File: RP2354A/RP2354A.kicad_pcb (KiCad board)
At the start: 2 copper layers, 40 x 80 mm, 66 parts, among them J101 USB4085-GF-A, J102 AudioJack2_SwitchT, J103 AudioJack2_SwitchT, J201 TC2030-NL, Q101 MMBF5103, SW201 SW_Push_DPDT, U201 RP2354A, U202 NCP1117-3.3_SOT223, U301 TAC5112, Y201 ABM8-272-T3

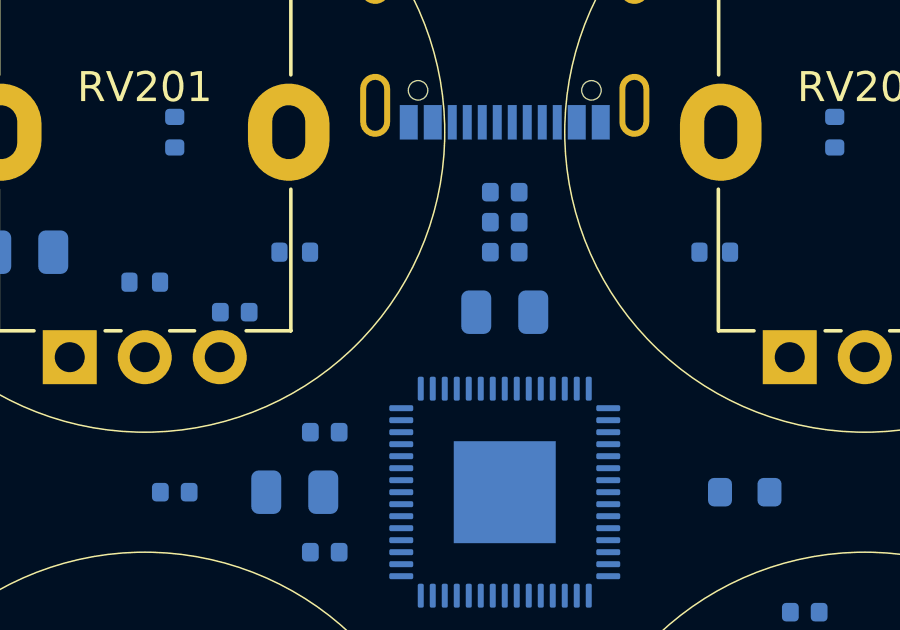
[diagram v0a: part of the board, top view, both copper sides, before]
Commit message: Update RP2354 board with proper inductor symbol
.. and fix up the LED simulation a bit too.  I simulate LEDs with the
built-in diode model, but with N ("emission coefficient") set to 3,
which gets me a forward voltage around 2V.

But I think I should change RS ("series resistance") instead (or in
addition to).  See

    https://led-ld.nichia.co.jp/api/data/spec/tech/SP-QR-C2-210932-2-E_The%20SPICE%20Model%20of%20LEDs.pdf

which talks much more about this.

I guess I don't care that much, I just wanted the current simulation for
the power LED to be in roughly the right ballpark.

The inductor change is the relatively important thing here.

Signed-off-by: Linus Torvalds <torvalds@linux-foundation.org>
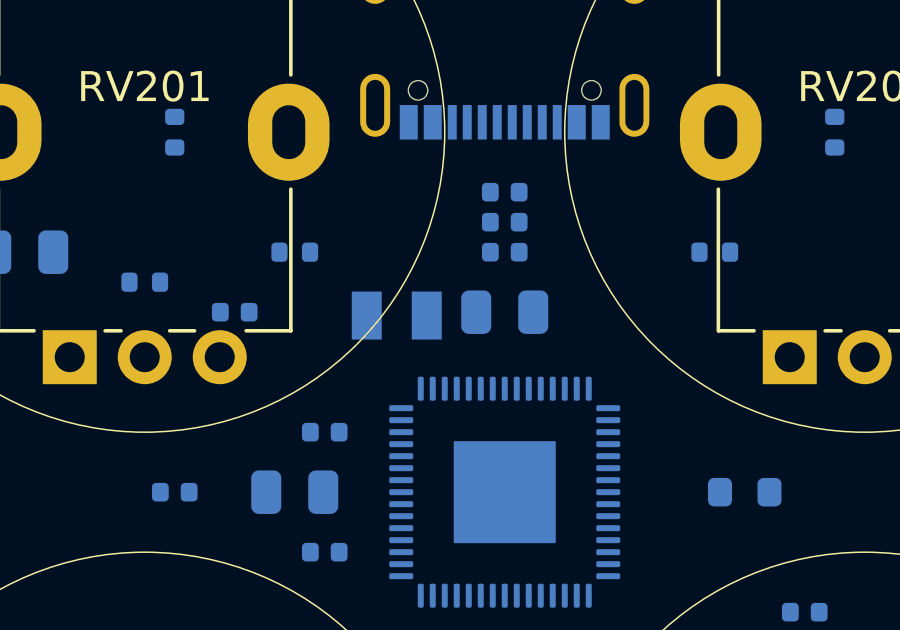
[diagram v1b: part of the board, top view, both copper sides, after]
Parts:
- added L201: 3.3u, Mylib:AOTA-B2016, B.Cu at (96.4, 84.1)
- turned C302 to 0 degrees
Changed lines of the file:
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@@
 			)
 		)
+		(property "Sim.Device" "D"
+			(at 0 0 0)
+			(unlocked yes)
+			(layer "F.Fab")
+			(hide yes)
+			(effects
+				(font
+					(size 1 1)
+					(thickness 0.15)
+				)
+			)
+		)
+		(property "Sim.Params" "n=3"
+			(at 0 0 0)
+			(unlocked yes)
+			(layer "F.Fab")
+			(hide yes)
+			(effects
+				(font
+					(size 1 1)
+					(thickness 0.15)
+				)
+			)
+		)
 		(property ki_fp_filters "LED* LED_SMD:* LED_THT:*")
 		(sheetname "/RPi/")
@@
 			)
 		)
-		(property "Sim.Params" "n=2.6"
+		(property "Sim.Params" "n=3"
 			(at 0 0 0)
 			(unlocked yes)
@@
 		(placed yes)
 		(layer "B.Cu")
-		(at 100 84 180)
+		(at 100 84)
 		(descr "Capacitor SMD 0805 (2012 Metric), square (rectangular) end terminal, IPC-7351 nominal, (Body size source: IPC-SM-782 page 76, https://www.pcb-3d.com/wordpress/wp-content/uploads/ipc-sm-782a_amendment_1_and_2.pdf, https://docs.google.com/spreadsheets/d/1BsfQQcO9C6DZCsRaXUlFlo91Tg2WpOkGARC1WS5S8t0/edit?usp=sharing), generated with kicad-footprint-generator")
 		(tags "capacitor")
@@
 		(attr smd)
 		(fp_line
-			(start -0.261252 0.735)
-			(end 0.261252 0.735)
+			(start -0.261252 -0.735)
+			(end 0.261252 -0.735)
 			(stroke
 				(width 0.12)
@@
 		)
 		(fp_line
-			(start -0.261252 -0.735)
-			(end 0.261252 -0.735)
+			(start -0.261252 0.735)
+			(end 0.261252 0.735)
 			(stroke
 				(width 0.12)
@@
 		)
 		(fp_line
-			(start 1.7 0.98)
-			(end 1.7 -0.98)
+			(start -1.7 -0.98)
+			(end -1.7 0.98)
 			(stroke
 				(width 0.05)
@@
 		)
 		(fp_line
-			(start 1.7 -0.98)
-			(end -1.7 -0.98)
+			(start -1.7 0.98)
+			(end 1.7 0.98)
 			(stroke
 				(width 0.05)
@@
 		)
 		(fp_line
-			(start -1.7 0.98)
-			(end 1.7 0.98)
+			(start 1.7 -0.98)
+			(end -1.7 -0.98)
 			(stroke
 				(width 0.05)
@@
 		)
 		(fp_line
-			(start -1.7 -0.98)
-			(end -1.7 0.98)
+			(start 1.7 0.98)
+			(end 1.7 -0.98)
 			(stroke
 				(width 0.05)
@@
 		)
 		(fp_line
-			(start 1 0.625)
-			(end 1 -0.625)
+			(start -1 -0.625)
+			(end -1 0.625)
 			(stroke
 				(width 0.1)
@@
 		)
 		(fp_line
-			(start 1 -0.625)
-			(end -1 -0.625)
+			(start -1 0.625)
+			(end 1 0.625)
 			(stroke
 				(width 0.1)
@@
 		)
 		(fp_line
-			(start -1 0.625)
-			(end 1 0.625)
+			(start 1 -0.625)
+			(end -1 -0.625)
 			(stroke
 				(width 0.1)
@@
 		)
 		(fp_line
-			(start -1 -0.625)
-			(end -1 0.625)
+			(start 1 0.625)
+			(end 1 -0.625)
 			(stroke
 				(width 0.1)
@@
 		)
 		(pad "1" smd roundrect
-			(at -0.95 0 180)
+			(at -0.95 0)
 			(size 1 1.45)
 			(layers "B.Cu" "B.Mask" "B.Paste")
@@
 		)
 		(pad "2" smd roundrect
-			(at 0.95 0 180)
+			(at 0.95 0)
 			(size 1 1.45)
 			(layers "B.Cu" "B.Mask" "B.Paste")
@@
 		)
 	)
+	(footprint "Mylib:AOTA-B2016"
+		(layer "B.Cu")
+		(at 96.4 84.1125 180)
+		(descr "Abracon Polarized Inductor 0806 (2016 metric)")
+		(tags "Inductor 0806 2016")
+		(property "Reference" "L201"
+			(at 0 2 0)
+			(unlocked yes)
+			(layer "B.SilkS")
+			(effects
+				(font
+					(size 1 1)
+					(thickness 0.1)
+				)
+				(justify mirror)
+			)
+		)
+		(property "Value" "3.3u"
+			(at 0 -1 0)
+			(unlocked yes)
+			(layer "B.Fab")
+			(effects
+				(font
+					(size 1 1)
+					(thickness 0.15)
+				)
+				(justify mirror)
+			)
+		)
+		(property "Datasheet" "https://abracon.com/datasheets/AOTA-B201610S3R3-101-T.pdf"
+			(at 0 0 0)
+			(unlocked yes)
+			(layer "B.Fab")
+			(hide yes)
+			(effects
+				(font
+					(size 1 1)
+					(thickness 0.15)
+				)
+				(justify mirror)
+			)
+		)
+		(property "Description" "Inductor"
+			(at 0 0 0)
+			(unlocked yes)
+			(layer "B.Fab")
+			(hide yes)
+			(effects
+				(font
+					(size 1 1)
+					(thickness 0.15)
+				)
+				(justify mirror)
+			)
+		)
+		(property ki_fp_filters "Choke_* *Coil* Inductor_* L_*")
+		(sheetname "/RPi/")
+		(sheetfile "rpi2354.kicad_sch")
+		(attr smd)
+		(fp_circle
+			(center -0.9 1.3)
+			(end -0.75 1.3)
+			(stroke
+				(width 0.1)
+				(type solid)
+			)
+			(fill yes)
+			(layer "B.SilkS")
+		)
+		(fp_rect
+			(start -1.65 1.05)
+			(end 1.65 -1.05)
+			(stroke
+				(width 0.05)
+				(type solid)
+			)
+			(fill no)
+			(layer "B.CrtYd")
+		)
+		(fp_text user "${REFERENCE}"
+			(at 0 -2.5 0)
+			(unlocked yes)
+			(layer "B.Fab")
+			(effects
+				(font
+					(size 1 1)
+					(thickness 0.15)
+				)
+				(justify mirror)
+			)
+		)
+		(pad "1" smd rect
+			(at -1 0 180)
+			(size 1 1.6)
+			(layers "B.Cu" "B.Mask" "B.Paste")
+			(net 10 "+1V1")
+			(pinfunction "1")
+			(pintype "passive")
+		)
+		(pad "2" smd rect
+			(at 1 0 180)
+			(size 1 1.6)
+			(layers "B.Cu" "B.Mask" "B.Paste")
+			(net 53 "/RPi/VREG_LX")
+			(pinfunction "2")
+			(pintype "passive")
+		)
+		(embedded_fonts no)
+	)
 	(footprint "Capacitor_SMD:C_0805_2012Metric"

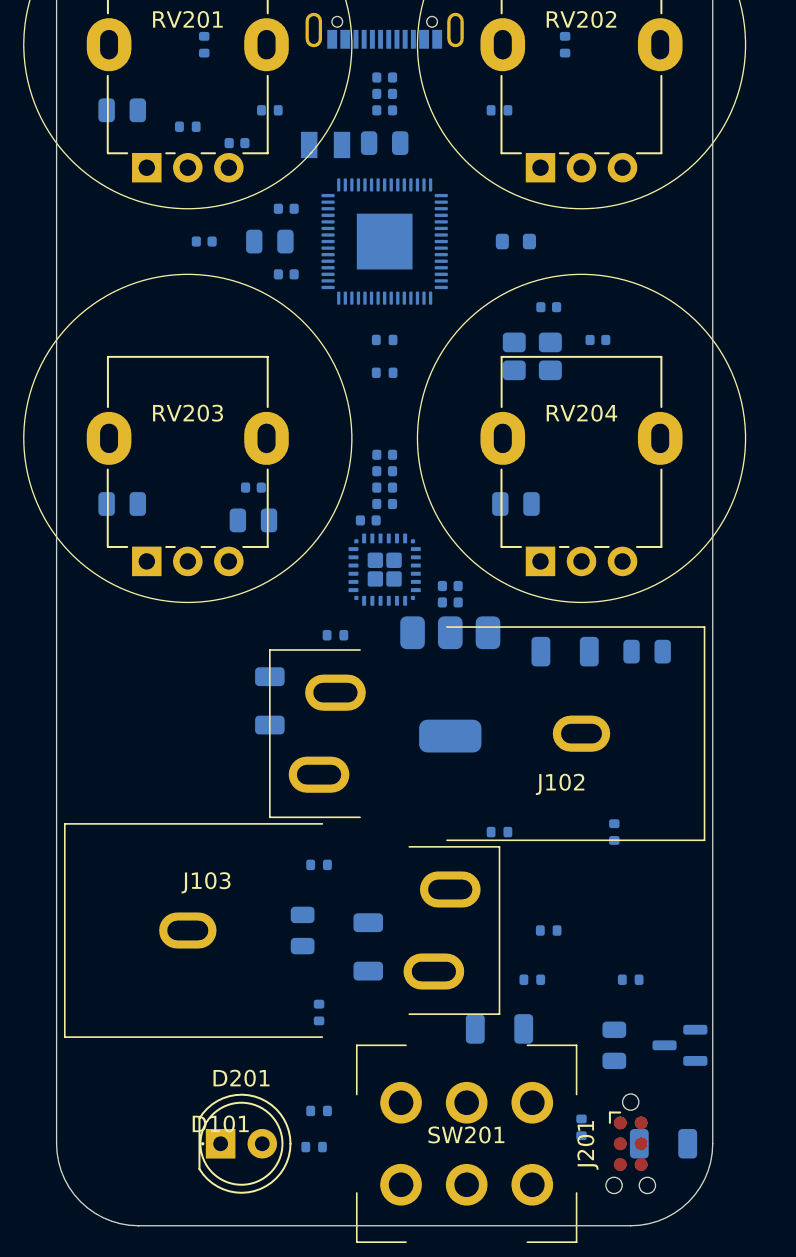
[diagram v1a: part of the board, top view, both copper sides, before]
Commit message: First cut at BOM selection for caps and resistors
The size choices were a bit random, this standardizes on 0402 for
resistors.  Also, optimize the BOM by just sharing values where they
don't matter that much.

For example, we need those 5k1 resistors for the USB CC pulldowns, and
we might as well then use that for the i2c pullup resistors too.  And
the self-biasing source resistor for the JFET input could use the same.

For similar reasons, just standardize on 33R for the low value resistors
that we use for the USB data line serial termination and the analog
voltage RC filtering.

Capacitors are 0402 for small values (0.1uF and smaller) or 0603 for
bigger capacitance values.  That seems to match availability.

Signed-off-by: Linus Torvalds <torvalds@linux-foundation.org>
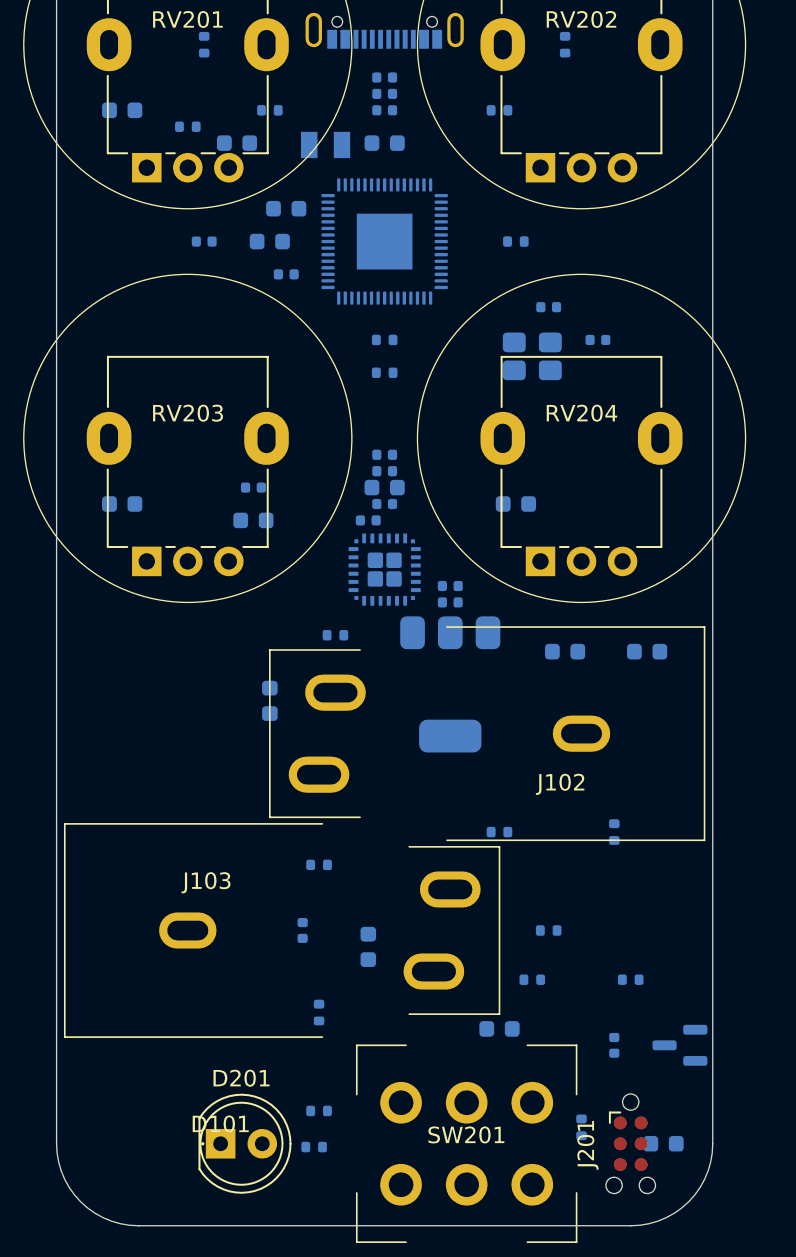
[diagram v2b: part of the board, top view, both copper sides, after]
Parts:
- C101, C103, C105, C106, C107: footprint Capacitor_SMD:C_1206_3216Metric -> Capacitor_SMD:C_0603_1608Metric
- C102, C104: footprint Capacitor_SMD:C_0805_2012Metric -> Capacitor_SMD:C_0402_1005Metric
- C201, C202: value 4.7u -> 4.7uF; footprint Capacitor_SMD:C_0805_2012Metric -> Capacitor_SMD:C_0603_1608Metric
- C203, C206, C207, C208, C209, C210, C211, C212, C213: value 100n -> 0.1uF
- C204, C205: value 4.7u -> 4.7uF; footprint Capacitor_SMD:C_0402_1005Metric -> Capacitor_SMD:C_0603_1608Metric
- C214, C215: value 15p -> 15pF
- C216, C217: value 10u -> 10uF; footprint Capacitor_SMD:C_0805_2012Metric -> Capacitor_SMD:C_0603_1608Metric
- C301, C302, C305: footprint Capacitor_SMD:C_0805_2012Metric -> Capacitor_SMD:C_0603_1608Metric
- C307: footprint Capacitor_SMD:C_0402_1005Metric -> Capacitor_SMD:C_0603_1608Metric
- L201: value 3.3u -> 3.3uH
- R106, R107: value 3k3 -> 5k1
- R110: value 100R -> 33R
- R201: value 33 -> 33R
- R205: renamed from R204; value 27R -> 33R
- R206: renamed from R205; value 27R -> 33R
- R208: renamed from R207; value 3k3 -> 5k1
- R209: renamed from R208; value 3k3 -> 5k1; footprint Resistor_SMD:R_0603_1608Metric -> Resistor_SMD:R_0402_1005Metric
- renumbered R209 to R204, R206 to R207

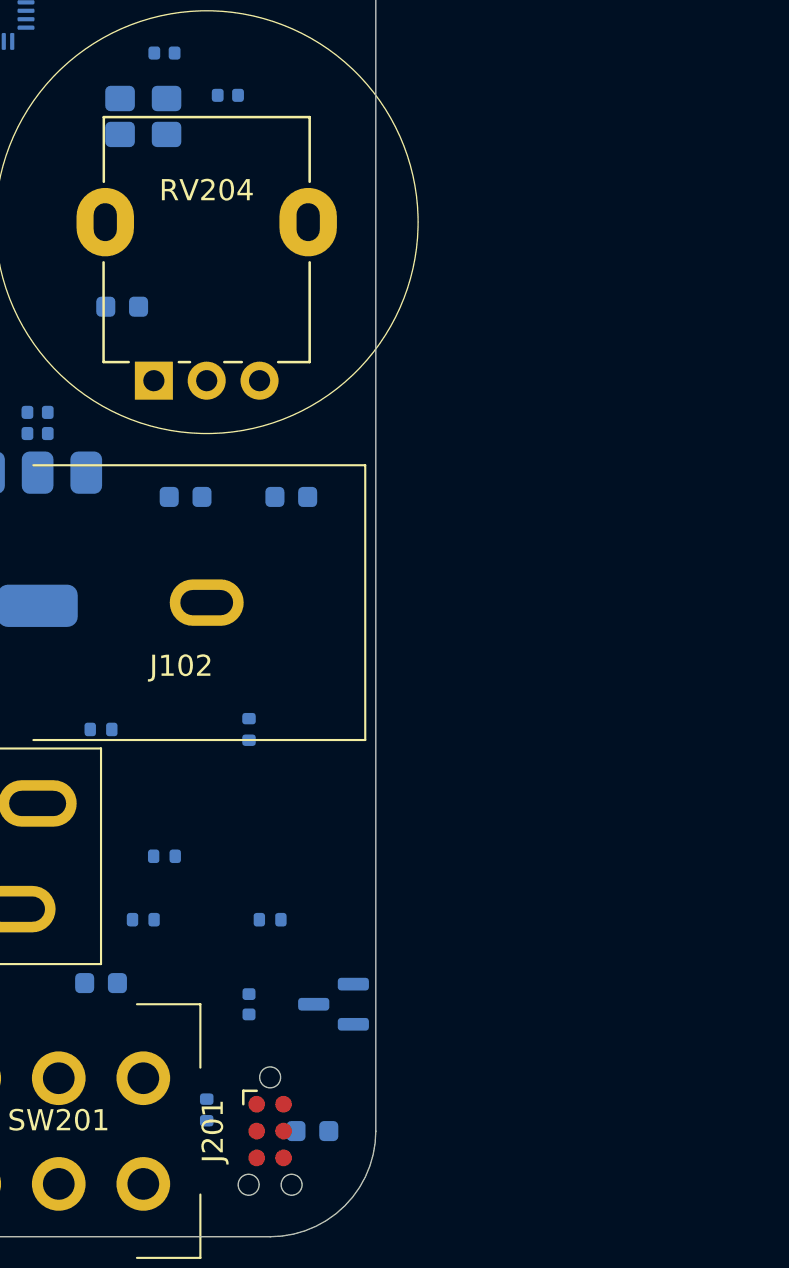
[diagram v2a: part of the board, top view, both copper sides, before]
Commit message: Switch the MMBF5103 JFET over to a OPA365 op amp
This is a long time coming, but it was triggered by jlcpcb not stocking
the MMBF5103, and all the alternatives looked worse.  So I guess sanity
has to prevail, and I should use an opamp rather than a discrete JFET
input stage.

I looked at the J201 - which I have tested and works, but has a
potentially very low V_{GSOFF} that will cause clipping.  And the
MMBFJ309L looked good in simulation and had better parameter values, but
I've never tested it, so it seemed a bit risky particularly since the
intended market seems to be for much higher frequency circuits.

I even looked at the JFE150, which is another silly-expensive thing sold
to audio markets.  I guess that tracks.

In the end, a plain simple opamp is definitely the sane choice.

To rebias the incoming signal, this uses the MICBIAS from the TAC5112,
which is typically 2.75V (but can be programmed to 2.5V or turned off
entirely etc).  It's there, it's almost what it is meant for, so let's
use it.

The OPA365 looks fine, and does rail-to-rail input and output and can do
single supplies down to 2.2V, but rather than put even more on the 3.3V
rail (and limiting the voltage swing), this just uses the 5V USB VBUS
power supply.

This does have some minimal caps for filtering (replacing the old +VA
supply to the JFET) but the OPA365 also claims good PSRR.

This all does seem like the right thing to do, but I'm still a bit sad
since the discrete JFET was just more interesting.

Signed-off-by: Linus Torvalds <torvalds@linux-foundation.org>
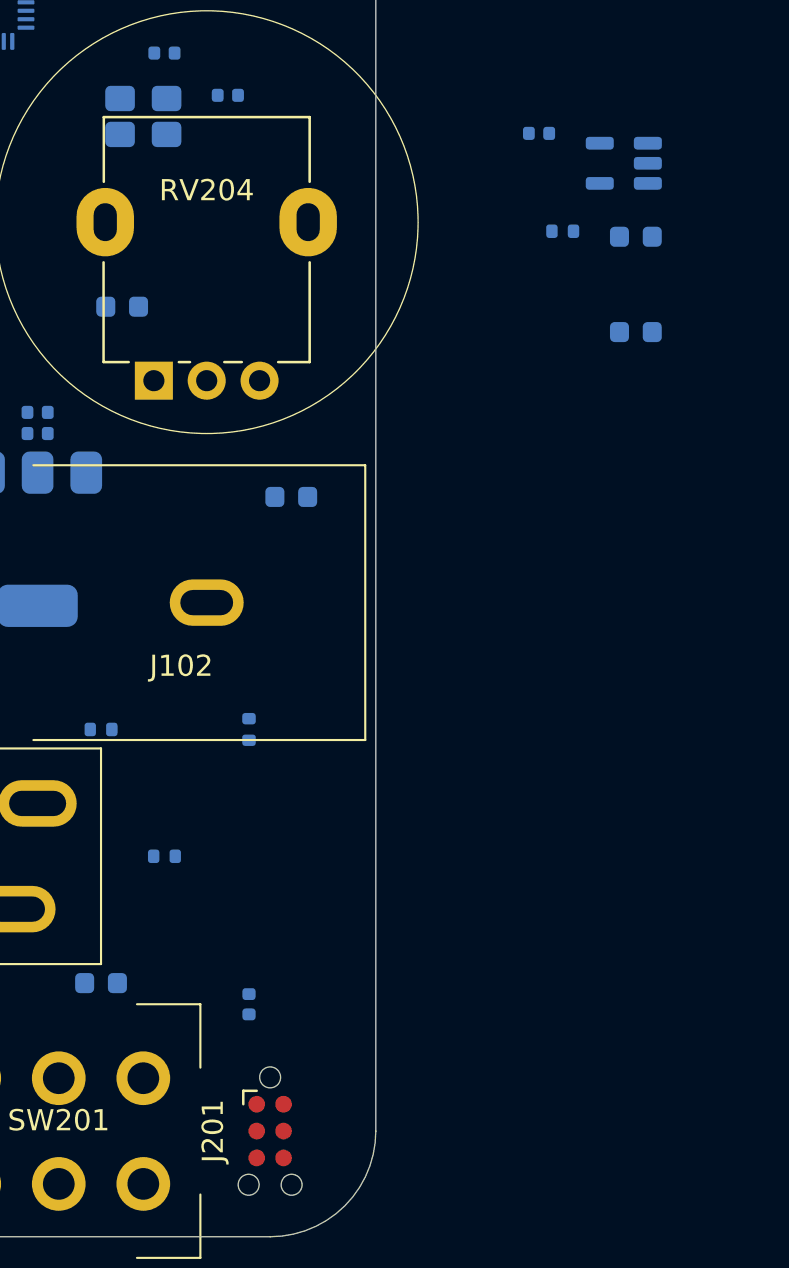
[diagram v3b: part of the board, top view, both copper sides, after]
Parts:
- removed the C106 at (111.0, 115.0)
- removed the C107 at (117.0, 145.0)
- removed Q101: MMBF5103, Package_TO_SOT_SMD:SOT-23
- removed the R105 at (115.0, 135.0)
- removed the R106 at (109.0, 135.0)
- removed R110: 33R, Resistor_SMD:R_0402_1005Metric
- added C103: 10uF, Capacitor_SMD:C_0603_1608Metric, B.Cu at (132.3, 102.7)
- added C105: 0.1uF, Capacitor_SMD:C_0402_1005Metric, B.Cu at (127.7, 97.8)
- added C308: 1uF, Capacitor_SMD:C_0603_1608Metric, B.Cu at (132.3, 107.2)
- added R102: 1MEG, Resistor_SMD:R_0402_1005Metric, B.Cu at (128.8, 102.4)
- added U101: OPA365xxDBV, Package_TO_SOT_SMD:SOT-23-5, B.Cu at (131.7, 99.2)
- renumbered C103 to C104, C104 to C106, C105 to C107, R102 to R103, R103 to R104, R104 to R105, R107 to R106, R108 to R107, R109 to R108
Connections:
- U301 pad 14: unconnected-(U301-MICBIAS-Pad14) -> VBIAS
